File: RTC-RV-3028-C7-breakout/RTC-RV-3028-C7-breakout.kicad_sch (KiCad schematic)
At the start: 12 parts, among them J1 Conn_01x04_Female, J2 Conn_01x04_Female, U1 RV-3028-C7

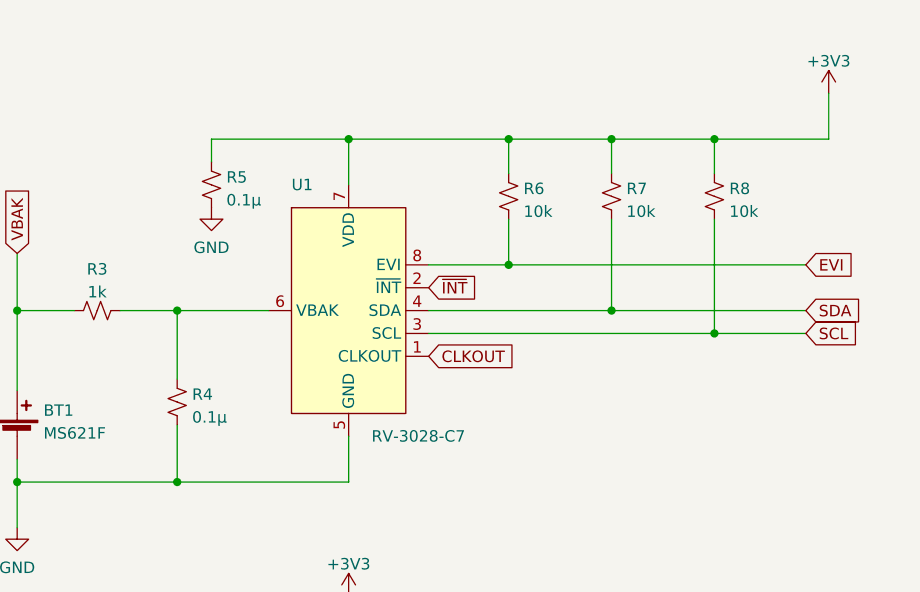
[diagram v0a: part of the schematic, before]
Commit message: Fix mis-labeled components
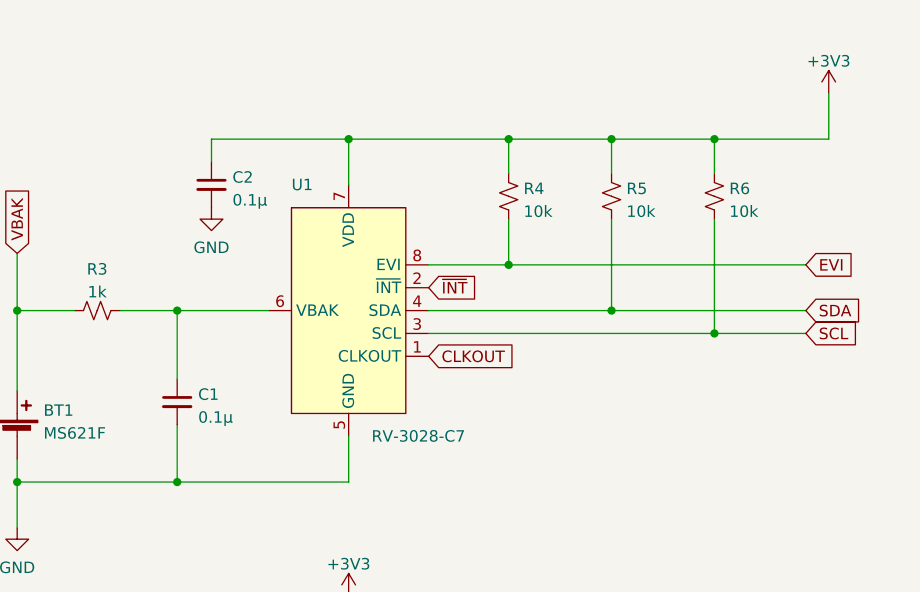
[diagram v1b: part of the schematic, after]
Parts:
- removed R4, R5: 0.1µ, Resistor_SMD:R_0603_1608Metric, symbol Device:R_Small_US
- added C1, C2: 0.1µ, Capacitor_SMD:C_0603_1608Metric, symbol Device:C_Small
- renumbered R6 to R4, R7 to R5, R8 to R6
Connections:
- net +3V3: now also C2.1
- net GND: now also C1.2, C2.2
- net at R3.2, U1.6 (VBAK): now also C1.1
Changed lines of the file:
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@@
   (symbol (lib_id "Device:R_Small_US") (at 227.33 86.36 180) (unit 1)
     (in_bom yes) (on_board yes) (fields_autoplaced)
-    (property "Reference" "R7" (id 0) (at 228.981 85.5253 0)
+    (property "Reference" "R5" (id 0) (at 228.981 85.5253 0)
       (effects (font (size 1.27 1.27)) (justify right))
     )
@@
     (pin "2")
   )
-  (symbol (lib_id "Device:R_Small_US") (at 179.07 109.22 0) (unit 1)
-    (in_bom yes) (on_board yes) (fields_autoplaced)
-    (property "Reference" "R4" (id 0) (at 180.721 108.3853 0)
-      (effects (font (size 1.27 1.27)) (justify left))
-    )
-    (property "Value" "0.1µ" (id 1) (at 180.721 110.9222 0)
-      (effects (font (size 1.27 1.27)) (justify left))
-    )
-    (property "Footprint" "Resistor_SMD:R_0603_1608Metric" (id 2) (at 179.07 109.22 0)
-      (effects (font (size 1.27 1.27)) hide)
-    )
-    (property "Datasheet" "~" (id 3) (at 179.07 109.22 0)
+  (symbol (lib_id "Device:C_Small") (at 182.88 85.09 0) (unit 1)
+    (in_bom yes) (on_board yes) (fields_autoplaced)
+    (property "Reference" "C2" (id 0) (at 185.2041 84.2616 0)
+      (effects (font (size 1.27 1.27)) (justify left))
+    )
+    (property "Value" "0.1µ" (id 1) (at 185.2041 86.7985 0)
+      (effects (font (size 1.27 1.27)) (justify left))
+    )
+    (property "Footprint" "Capacitor_SMD:C_0603_1608Metric" (id 2) (at 182.88 85.09 0)
+      (effects (font (size 1.27 1.27)) hide)
+    )
+    (property "Datasheet" "~" (id 3) (at 182.88 85.09 0)
       (effects (font (size 1.27 1.27)) hide)
     )
@@
   (symbol (lib_id "Device:R_Small_US") (at 238.76 86.36 180) (unit 1)
     (in_bom yes) (on_board yes) (fields_autoplaced)
-    (property "Reference" "R8" (id 0) (at 240.411 85.5253 0)
+    (property "Reference" "R6" (id 0) (at 240.411 85.5253 0)
       (effects (font (size 1.27 1.27)) (justify right))
     )
@@
     (pin "2")
   )
+  (symbol (lib_id "Device:C_Small") (at 179.07 109.22 0) (unit 1)
+    (in_bom yes) (on_board yes) (fields_autoplaced)
+    (property "Reference" "C1" (id 0) (at 181.3941 108.3916 0)
+      (effects (font (size 1.27 1.27)) (justify left))
+    )
+    (property "Value" "0.1µ" (id 1) (at 181.3941 110.9285 0)
+      (effects (font (size 1.27 1.27)) (justify left))
+    )
+    (property "Footprint" "Capacitor_SMD:C_0603_1608Metric" (id 2) (at 179.07 109.22 0)
+      (effects (font (size 1.27 1.27)) hide)
+    )
+    (property "Datasheet" "~" (id 3) (at 179.07 109.22 0)
+      (effects (font (size 1.27 1.27)) hide)
+    )
+    (pin "1")
+    (pin "2")
+  )
   (symbol (lib_id "Connector:Conn_01x04_Female") (at 252.73 140.97 0) (unit 1)
     (in_bom yes) (on_board yes) (fields_autoplaced)
@@
     (pin "3")
     (pin "4")
-  )
-  (symbol (lib_id "Device:R_Small_US") (at 182.88 85.09 0) (unit 1)
-    (in_bom yes) (on_board yes) (fields_autoplaced)
-    (property "Reference" "R5" (id 0) (at 184.531 84.2553 0)
-      (effects (font (size 1.27 1.27)) (justify left))
-    )
-    (property "Value" "0.1µ" (id 1) (at 184.531 86.7922 0)
-      (effects (font (size 1.27 1.27)) (justify left))
-    )
-    (property "Footprint" "Resistor_SMD:R_0603_1608Metric" (id 2) (at 182.88 85.09 0)
-      (effects (font (size 1.27 1.27)) hide)
-    )
-    (property "Datasheet" "~" (id 3) (at 182.88 85.09 0)
-      (effects (font (size 1.27 1.27)) hide)
-    )
-    (pin "1")
-    (pin "2")
   )
   (symbol (lib_id "power:+3V3") (at 198.12 130.81 0) (unit 1)
@@
   (symbol (lib_id "Device:R_Small_US") (at 215.9 86.36 0) (unit 1)
     (in_bom yes) (on_board yes) (fields_autoplaced)
-    (property "Reference" "R6" (id 0) (at 217.551 85.5253 0)
+    (property "Reference" "R4" (id 0) (at 217.551 85.5253 0)
       (effects (font (size 1.27 1.27)) (justify left))
     )
@@
       (reference "BT1") (unit 1) (value "MS621F") (footprint "Battery:BatteryHolder_Seiko_MS621F")
     )
+    (path "/53f1b64c-61f7-4340-b4ea-3bfa4cadc0be"
+      (reference "C1") (unit 1) (value "0.1µ") (footprint "Capacitor_SMD:C_0603_1608Metric")
+    )
+    (path "/3e8a6566-946d-4293-983b-718a46a1e19c"
+      (reference "C2") (unit 1) (value "0.1µ") (footprint "Capacitor_SMD:C_0603_1608Metric")
+    )
     (path "/933bdcc7-aa9f-4a74-9099-d07fbd6e7e34"
       (reference "J1") (unit 1) (value "Conn_01x04_Female") (footprint "Connector_PinSocket_2.54mm:PinSocket_1x04_P2.54mm_Vertical")
@@
       (reference "R3") (unit 1) (value "1k") (footprint "Resistor_SMD:R_0603_1608Metric")
     )
-    (path "/284e5962-152d-4bd3-a18a-94678804a8a4"
-      (reference "R4") (unit 1) (value "0.1µ") (footprint "Resistor_SMD:R_0603_1608Metric")
-    )
-    (path "/5d9a417d-7b5e-4671-8259-45a3eadaca6c"
-      (reference "R5") (unit 1) (value "0.1µ") (footprint "Resistor_SMD:R_0603_1608Metric")
-    )
     (path "/6cfc684e-8a30-4811-b7c5-232c33c6d48f"
+      (reference "R4") (unit 1) (value "10k") (footprint "Resistor_SMD:R_0603_1608Metric")
+    )
+    (path "/21473e18-959f-4c0f-b7e4-b0ac0ab36cd7"
+      (reference "R5") (unit 1) (value "10k") (footprint "Resistor_SMD:R_0603_1608Metric")
+    )
+    (path "/432fc41a-8d85-4773-b6d8-c4a55081f609"
       (reference "R6") (unit 1) (value "10k") (footprint "Resistor_SMD:R_0603_1608Metric")
     )
-    (path "/21473e18-959f-4c0f-b7e4-b0ac0ab36cd7"
-      (reference "R7") (unit 1) (value "10k") (footprint "Resistor_SMD:R_0603_1608Metric")
-    )
-    (path "/432fc41a-8d85-4773-b6d8-c4a55081f609"
-      (reference "R8") (unit 1) (value "10k") (footprint "Resistor_SMD:R_0603_1608Metric")
-    )
     (path "/111d7408-ae4a-48a6-b45f-50ce70cef96e"
